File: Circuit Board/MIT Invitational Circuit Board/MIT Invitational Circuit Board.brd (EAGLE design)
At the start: 228.9 x 60.9 mm, 362 parts, among them IC1101 7805DT, IC1201 7805DT, IC1301 7805DT, IC1501 7805DT, J1005 ICSP_HEADER, J1104 ICSP_HEADER, J1204 ICSP_HEADER, J1304 ICSP_HEADER, J204 ICSP_HEADER, J301 ICSP_HEADER, J401 ICSP_HEADER, J503 ICSP_HEADER, J603 ICSP_HEADER, J703 ICSP_HEADER, J704 ICSP_HEADER, J903 ICSP_HEADER, Q1001 PSMN7R0-60YS, Q1401 PSMN7R0-60YS, Q201 PSMN7R0-60YS, Q301 500mA/300V, Q401 500mA/300V, Q501 PSMN7R0-60YS, Q601 PSMN7R0-60YS, Q801 PSMN7R0-60YS, Q901 PSMN7R0-60YS, U1001 ATTINY25-20SSUR, U1002 MIC5205, U101 74HC1G04, U102 MIC5205, U1101 DRV8835, U1102 ATTINY25-20SSUR, U1201 DRV8835, U1202 ATTINY25-20SSUR, U1301 DRV8835, U1302 ATTINY25-20SSUR, U1401 74HC1G04, U1402 MIC5205, U201 74HC1G04, U202 ATTINY25-20SSUR, U203 MIC5205, U301 74HC1G04, U302 SN74*C1G08-DCK, U303 ATTINY25-20SSUR, U304 MIC5205, U401 74HC1G04, U402 SN74*C1G08-DCK, U403 ATTINY25-20SSUR, U404 MIC5205, U501 74HC1G04, U502 SN74*C1G08-DCK, U503 ATTINY25-20SSUR, U504 MIC5205, U601 74HC1G04, U602 SN74*C1G08-DCK, U603 ATTINY25-20SSUR, U604 MIC5205, U701 ATTINY25-20SSUR, U702 ATTINY25-20SSUR, U703 MIC5205, U801 74HC1G04, U802 SN74*C1G08-DCK, U803 MIC5205, U901 ATTINY25-20SSUR, U902 MIC5205, X1601 MSTBA2

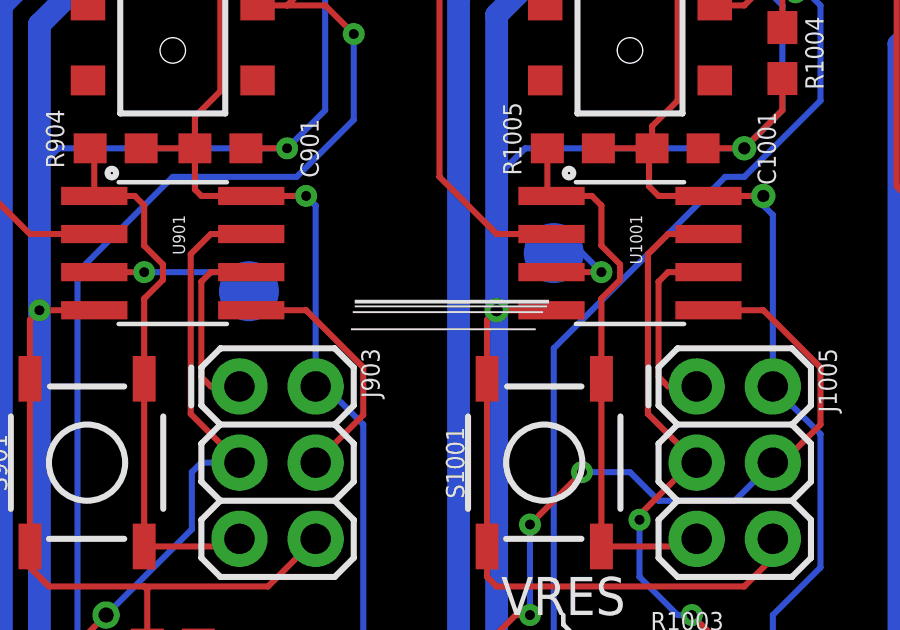
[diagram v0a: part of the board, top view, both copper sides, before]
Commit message: Reorganized files and updated schematics
MIT schematics have been finalized and the code is pretty stable, beisdes some thresholding issues.
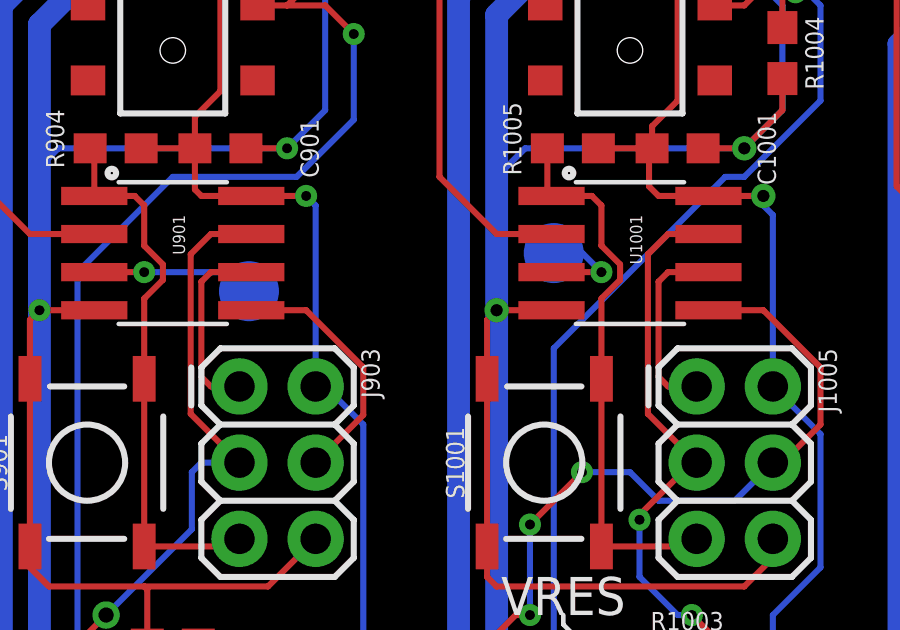
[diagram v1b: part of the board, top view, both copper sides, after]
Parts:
- R1004: value 10K -> 1M
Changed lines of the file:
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@@
 <?xml version="1.0" encoding="utf-8"?>
 <!DOCTYPE eagle SYSTEM "eagle.dtd">
-<eagle version="8.5.1">
+<eagle version="8.5.2">
 <drawing>
 <settings>
@@
 <text x="200.025" y="55.88" size="2.54" layer="21" font="vector">IMA 0.5</text>
 <text x="219.71" y="57.785" size="1.27" layer="21" font="vector">END</text>
-<rectangle x1="135.47851875" y1="29.81325" x2="141.63801875" y2="29.87675" layer="21"/>
-<rectangle x1="135.53948125" y1="30.38475" x2="141.88948125" y2="30.44825" layer="21"/>
-<rectangle x1="135.60298125" y1="30.57525" x2="142.01648125" y2="30.63875" layer="21"/>
-<rectangle x1="135.60298125" y1="30.70225" x2="142.08251875" y2="30.76575" layer="21"/>
-<rectangle x1="135.60298125" y1="30.76575" x2="142.08251875" y2="30.82925" layer="21"/>
 <wire x1="210.185" y1="15.24" x2="209.55" y2="14.605" width="0.1524" layer="21"/>
 <wire x1="209.55" y1="14.605" x2="209.55" y2="12.7" width="0.1524" layer="21"/>
@@
 <attribute name="VALUE" x="146.685" y="18.288" size="0.6096" layer="27" font="vector" ratio="20" align="top-center"/>
 </element>
-<element name="R1004" library="SparkFun-Resistors" package="0603" value="10K" x="149.86" y="39.0525" smashed="yes" rot="R270">
+<element name="R1004" library="SparkFun-Resistors" package="0603" value="1M" x="149.86" y="39.0525" smashed="yes" rot="R270">
 <attribute name="NAME" x="150.622" y="39.0525" size="0.6096" layer="25" font="vector" ratio="20" rot="R270" align="bottom-center"/>
 <attribute name="PROD_ID" value=" " x="149.86" y="39.0525" size="1.778" layer="27" rot="R270" display="off"/>
